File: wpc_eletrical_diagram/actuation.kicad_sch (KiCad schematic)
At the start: 8 parts, among them Q1 2N7000

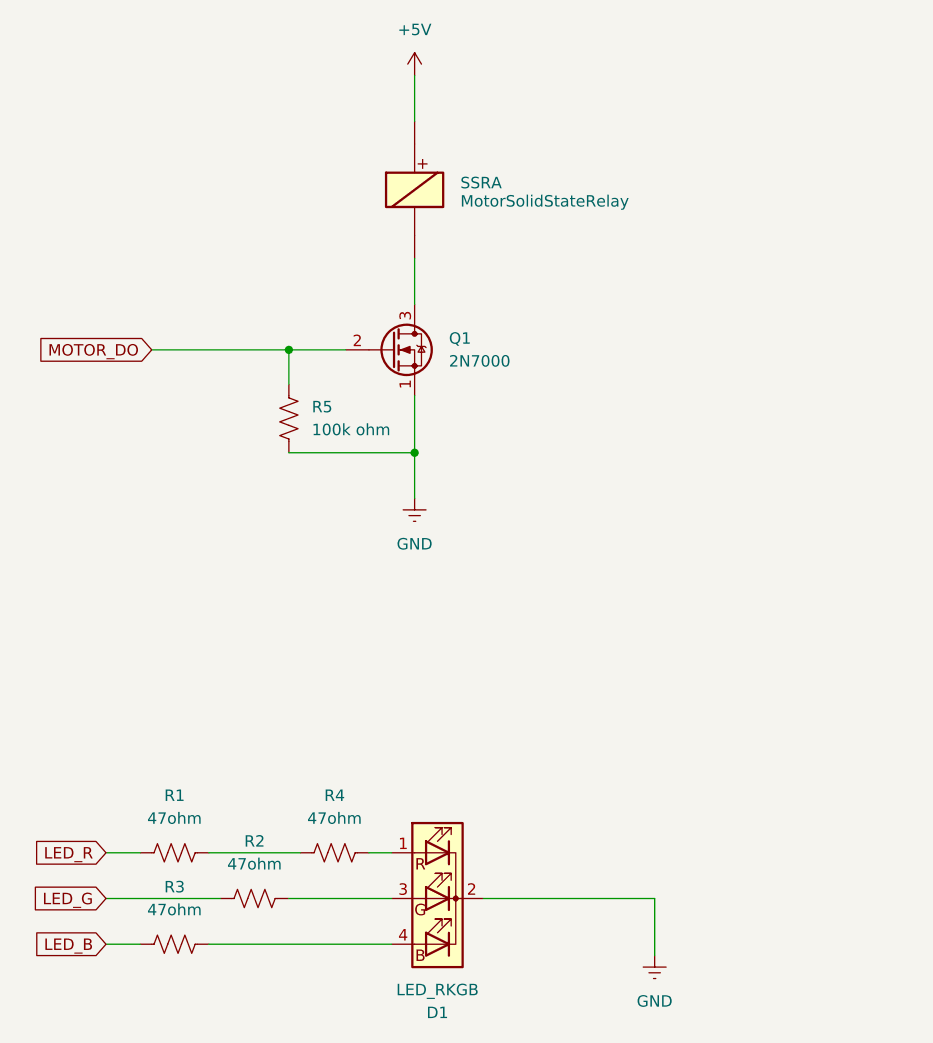
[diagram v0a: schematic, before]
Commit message: eletrical corrections
- schematic correction (sensors, actuation)
- main board correction (resistor values, chottky diodes) (v26)
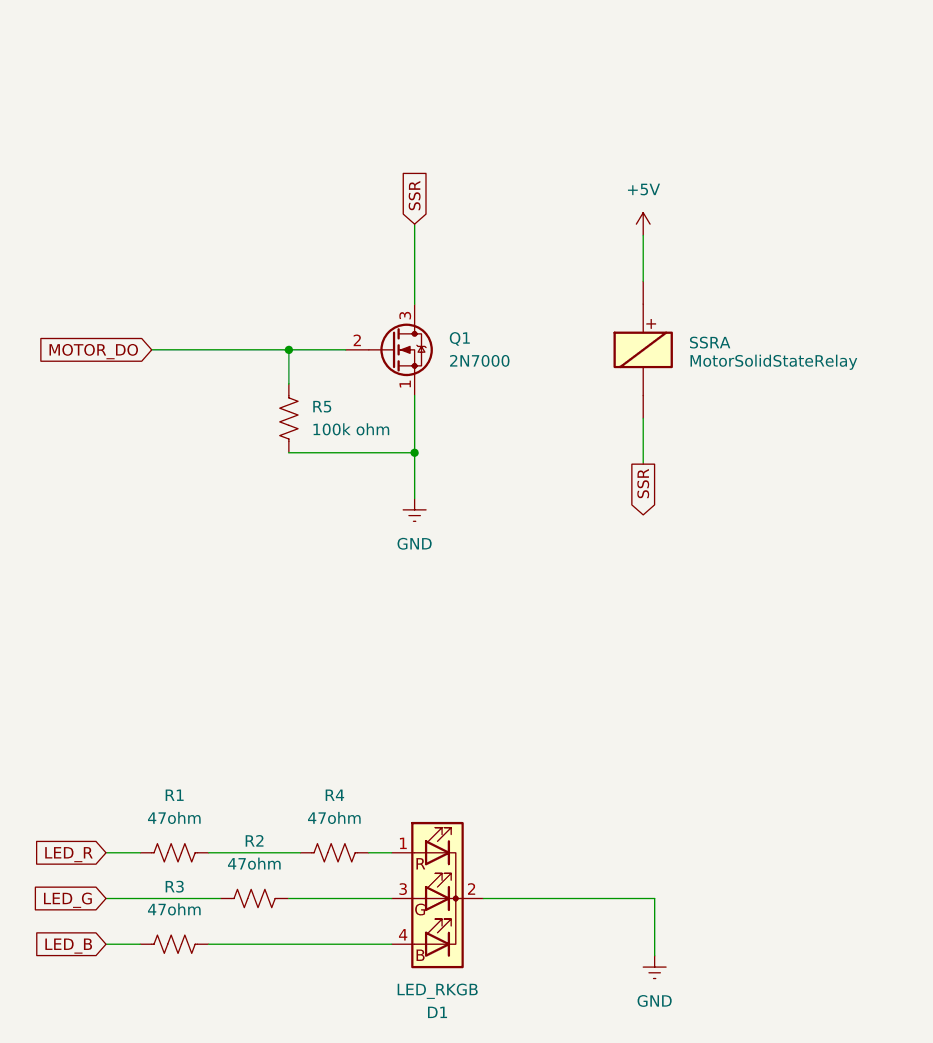
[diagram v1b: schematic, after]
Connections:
- net SSR: now reaches Q1.3 (D), SSR.A2
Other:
- moved on the sheet: SSRA
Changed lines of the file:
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@@
+	(wire
+		(pts
+			(xy 82.55 53.34) (xy 82.55 62.23)
+		)
+		(stroke
+			(width 0)
+			(type default)
+		)
+	)
 	(wire
 		(pts
@@
 	(wire
 		(pts
-			(xy 82.55 57.15) (xy 82.55 62.23)
+			(xy 107.95 74.93) (xy 107.95 80.01)
 		)
 		(stroke
@@
 	(wire
 		(pts
-			(xy 82.55 36.83) (xy 82.55 41.91)
+			(xy 107.95 54.61) (xy 107.95 59.69)
 		)
 		(stroke
@@
 		(property "Intersheetrefs" "${INTERSHEET_REFS}"
 			(at 39.5901 123.19 0)
+			(effects
+				(font
+					(size 1.27 1.27)
+				)
+				(justify right)
+			)
+		)
+	)
+	(global_label "SSR"
+		(shape input)
+		(at 82.55 53.34 90)
+		(fields_autoplaced yes)
+		(effects
+			(font
+				(size 1.27 1.27)
+			)
+			(justify left)
+		)
+		(property "Intersheetrefs" "${INTERSHEET_REFS}"
+			(at 82.55 46.6658 90)
+			(effects
+				(font
+					(size 1.27 1.27)
+				)
+				(justify left)
+			)
+		)
+	)
+	(global_label "SSR"
+		(shape output)
+		(at 107.95 80.01 270)
+		(fields_autoplaced yes)
+		(effects
+			(font
+				(size 1.27 1.27)
+			)
+			(justify right)
+		)
+		(property "Intersheetrefs" "${INTERSHEET_REFS}"
+			(at 107.95 86.6842 90)
 			(effects
 				(font
@@
 	(symbol
 		(lib_id "Relay:COTO_3660_Split")
-		(at 82.55 49.53 0)
+		(at 107.95 67.31 0)
 		(unit 1)
 		(exclude_from_sim no)
@@
 		(dnp no)
 		(property "Reference" "SSR"
-			(at 87.63 48.768 0)
+			(at 113.03 66.548 0)
 			(effects
 				(font
@@
 		)
 		(property "Value" "MotorSolidStateRelay"
-			(at 87.63 50.7999 0)
+			(at 113.03 68.5799 0)
 			(effects
 				(font
@@
 		)
 		(property "Footprint" "Relay_THT:Relay_3PST_COTO_3660"
-			(at 87.63 52.07 0)
+			(at 113.03 69.85 0)
 			(effects
 				(font
@@
 		)
 		(property "Datasheet" "https://cotorelay.com/wp-content/uploads/2014/09/3600_series_reed_relay_datasheet.pdf"
-			(at 82.55 49.53 0)
+			(at 107.95 67.31 0)
 			(effects
 				(font
@@
 		)
 		(property "Description" "Low thermal EMF 3PST-NO reed relay, 150V 0.25A, similar to 3650 but with shared shield/contact, 30.48x16.76x12.06mm"
-			(at 82.55 49.53 0)
+			(at 107.95 67.31 0)
 			(effects
 				(font
@@
 	(symbol
 		(lib_id "power:+5V")
-		(at 82.55 36.83 0)
+		(at 107.95 54.61 0)
 		(unit 1)
 		(exclude_from_sim no)
@@
 		(fields_autoplaced yes)
 		(property "Reference" "#PWR017"
-			(at 82.55 40.64 0)
+			(at 107.95 58.42 0)
 			(effects
 				(font
@@
 		)
 		(property "Value" "+5V"
-			(at 82.55 31.75 0)
+			(at 107.95 49.53 0)
 			(effects
 				(font
@@
 		)
 		(property "Footprint" ""
-			(at 82.55 36.83 0)
+			(at 107.95 54.61 0)
 			(effects
 				(font
@@
 		)
 		(property "Datasheet" ""
-			(at 82.55 36.83 0)
+			(at 107.95 54.61 0)
 			(effects
 				(font
@@
 		)
 		(property "Description" "Power symbol creates a global label with name \"+5V\""
-			(at 82.55 36.83 0)
-			(effects
-				(font
+			(at 107.95 54.61 0)
+			(effects
+				(font
